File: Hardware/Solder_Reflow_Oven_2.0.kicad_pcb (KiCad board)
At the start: 2 copper layers, 64.8 x 61.2 mm, 46 parts, among them J1 Conn_01x02_Male, J2 USB_B, J3 Conn_01x02_Male, J4 Conn_02x03_Top_Bottom, J5 Conn_01x02_Top_Bottom, J6 Conn_01x02_Male, J7 Conn_01x24_Male, J8 Conn_01x02_Top_Bottom, Q1 2SD1805, SW1 SW_DIP_x01, U1 LM2940IMPX-10/NOPB, U2 MAX31855KASA, U3 RCLAMP0502A.TCT, U4 STM32L053R6T6, U5 CDBHD140L-G, U6 F24-100-C2, U7 SPDT_Reflow, U8 LD1117S33TR_SOT223, Y1 Crystal_GND24

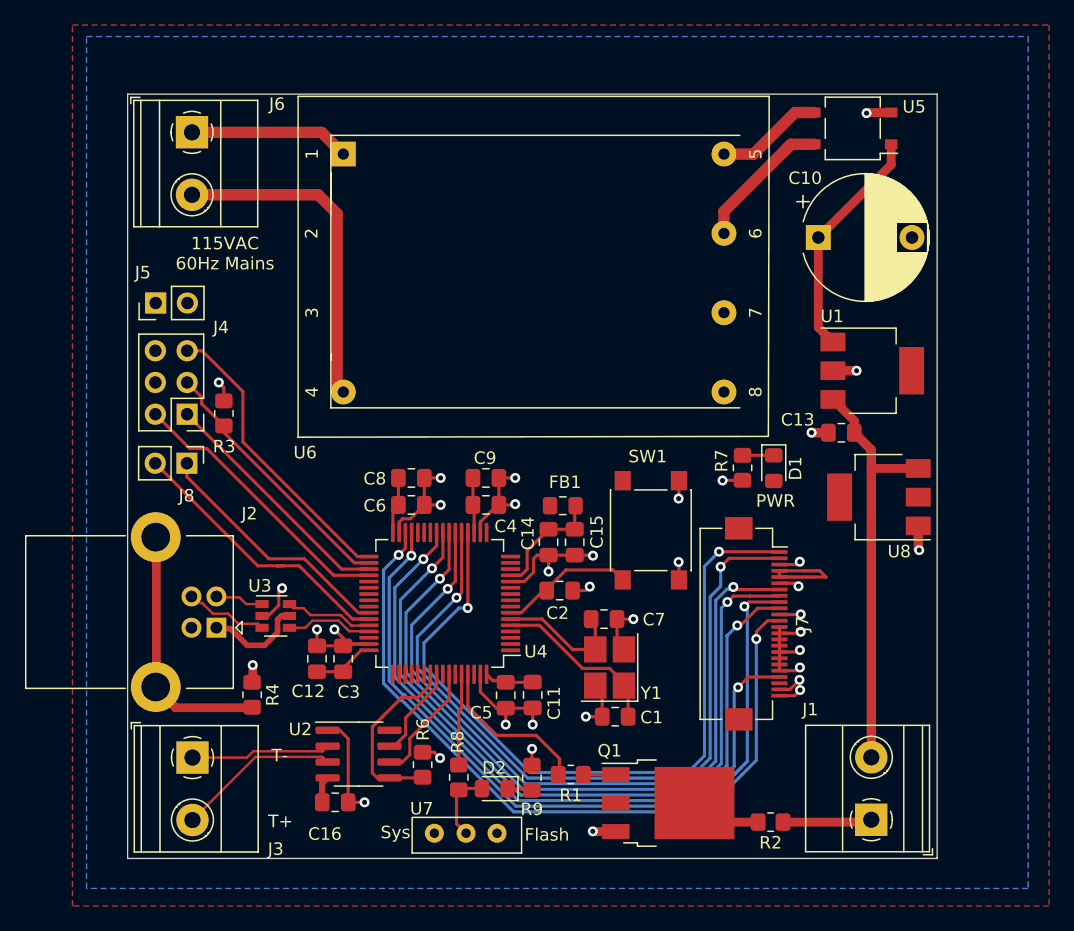
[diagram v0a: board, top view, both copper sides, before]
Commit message: Updating board to include mounting holes and debugging LED
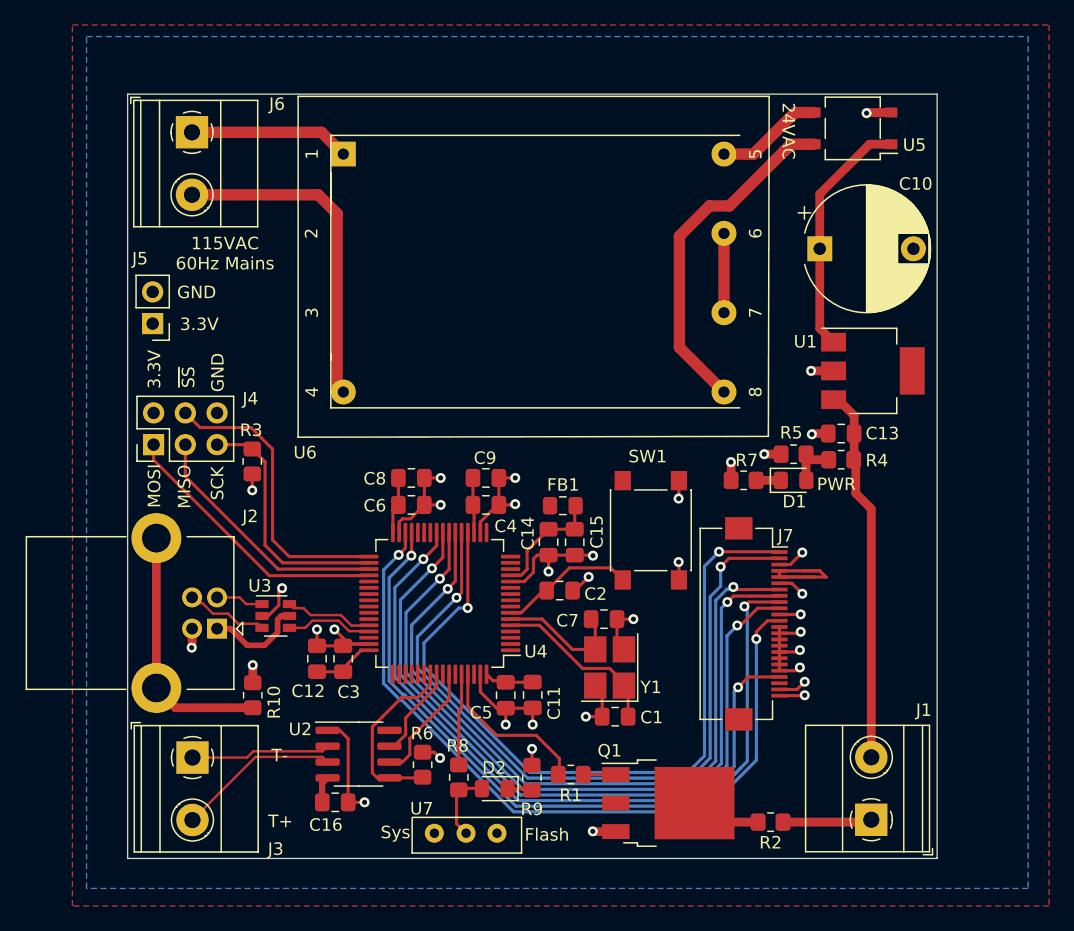
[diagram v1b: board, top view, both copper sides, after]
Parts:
- removed J8: Conn_01x02_Top_Bottom, Connector_PinHeader_2.54mm:PinHeader_1x02_P2.54mm_Vertical
- removed U8: LD1117S33TR_SOT223, Package_TO_SOT_SMD:SOT-223-3_TabPin2
- added R10: R, Resistor_SMD:R_0805_2012Metric_Pad1.20x1.40mm_HandSolder, F.Cu at (49.4, 121.8)
- added R5: 1k, Resistor_SMD:R_0805_2012Metric_Pad1.20x1.40mm_HandSolder, F.Cu at (92.7, 102.5)
- R4: value 10 -> 2k
- moved R4 50.8 mm to (96.5, 102.9), turned to 180 degrees
- moved R3 4.47 mm to (49.4, 103.1), turned to 270 degrees
- moved J4 3.62 mm to (41.5, 101.7), turned to 90 degrees
- moved D1 1.86 mm to (92.7, 104.6), turned to 0 degrees
- moved J5 1.67 mm to (41.4, 92.0), turned to 180 degrees
- moved R7 1.01 mm to (88.7, 104.6), turned to 0 degrees
- moved C10 0.91 mm to (94.8, 86.0)
- moved J2 0.09 mm to (46.5, 116.5)
- moved C13 0.06 mm to (96.5, 100.8)
- moved U1 0.05 mm to (99.1, 95.8)
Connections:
- J4 pad 1: SPI1_MISO -> SPI1_MOSI
- J4 pad 2: SPI1_MOSI -> VDD_3.3
- J4 pad 3: SPI1_SCK -> SPI1_MISO
- J4 pad 4: VSS -> SPI_NSS
- J4 pad 5: SPI_NSS -> SPI1_SCK
- J4 pad 6: VDD_3.3 -> VSS
- R4 pad 1: VSS -> VDD_10
- R4 pad 2: Net-(J2-Pad5) -> VDD_3.3
- U4 pad 42: USART1_TX -> Net-(U4-Pad42)
- U4 pad 43: USART1_RX -> Net-(U4-Pad43)
- U6 pad 6: Net-(U5-Pad4) -> Net-(U6-Pad6)
- U6 pad 7: Net-(U6-Pad7) -> Net-(U6-Pad6)
- U6 pad 8: Net-(U6-Pad8) -> Net-(U5-Pad4)
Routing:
- net USART1_RX: track 22.8 -> 0.00 mm
- net USART1_TX: track 20.2 -> 0.00 mm
- net Net-(U5-Pad4): track 11.9 -> 28.5 mm
- net Net-(U6-Pad6): track 0.00 -> 6.35 mm
- net VDD_3.3: track 33.7 -> 37.8 mm
- net VDD_10: track 33.7 -> 30.1 mm
- net VSS: track 101.7 -> 103.9 mm, vias 35 -> 36
- net SPI1_SCK: track 21.2 -> 20.0 mm
- net Net-(C10-Pad1): track 18.7 -> 19.7 mm
- net SPI1_MISO: track 19.7 -> 20.3 mm
- net Net-(D1-Pad1): track 2.50 -> 1.98 mm
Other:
- board text added: "24VAC"
- board text removed: "RX"
- board text removed: "TX"
